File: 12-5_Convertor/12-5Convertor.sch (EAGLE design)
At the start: 19 parts, among them IC1 ACS764, U1 LM2678

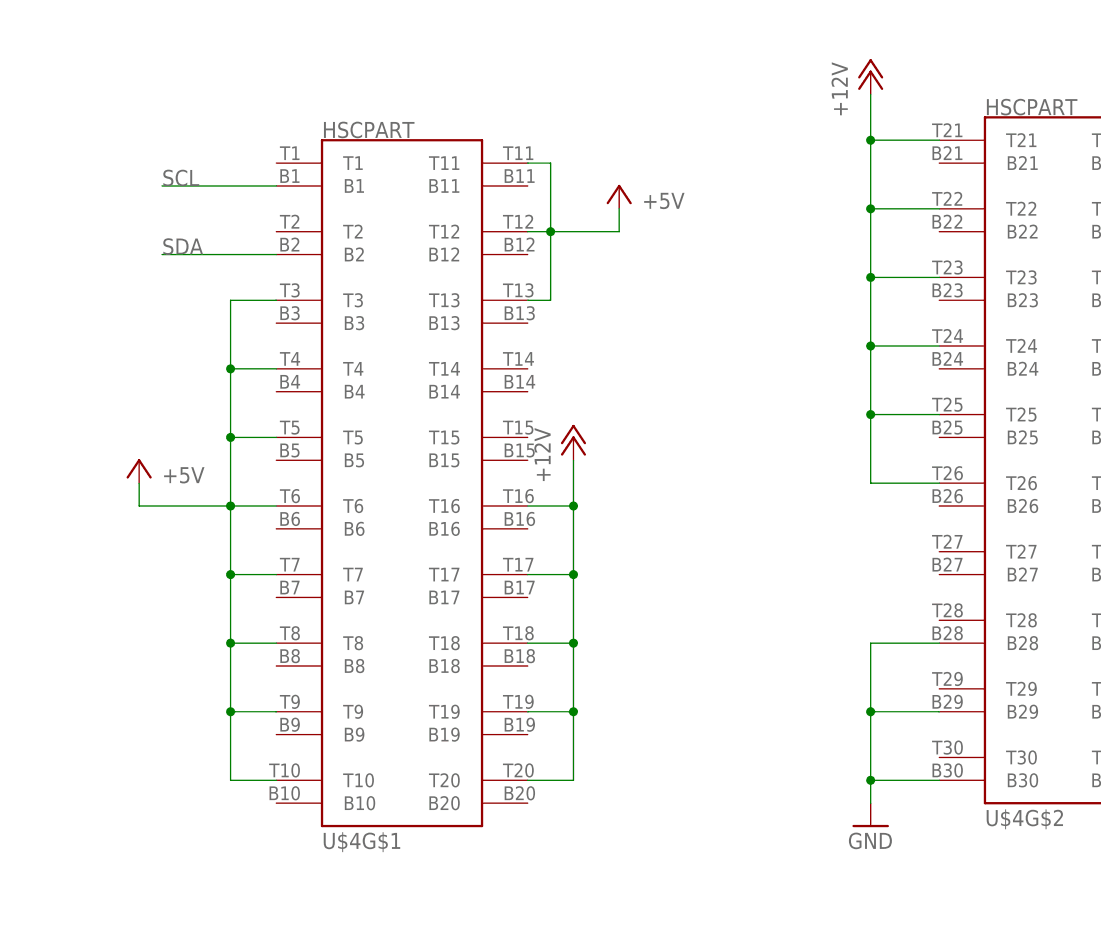
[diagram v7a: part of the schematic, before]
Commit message: Changed the pin order of the backplane connector
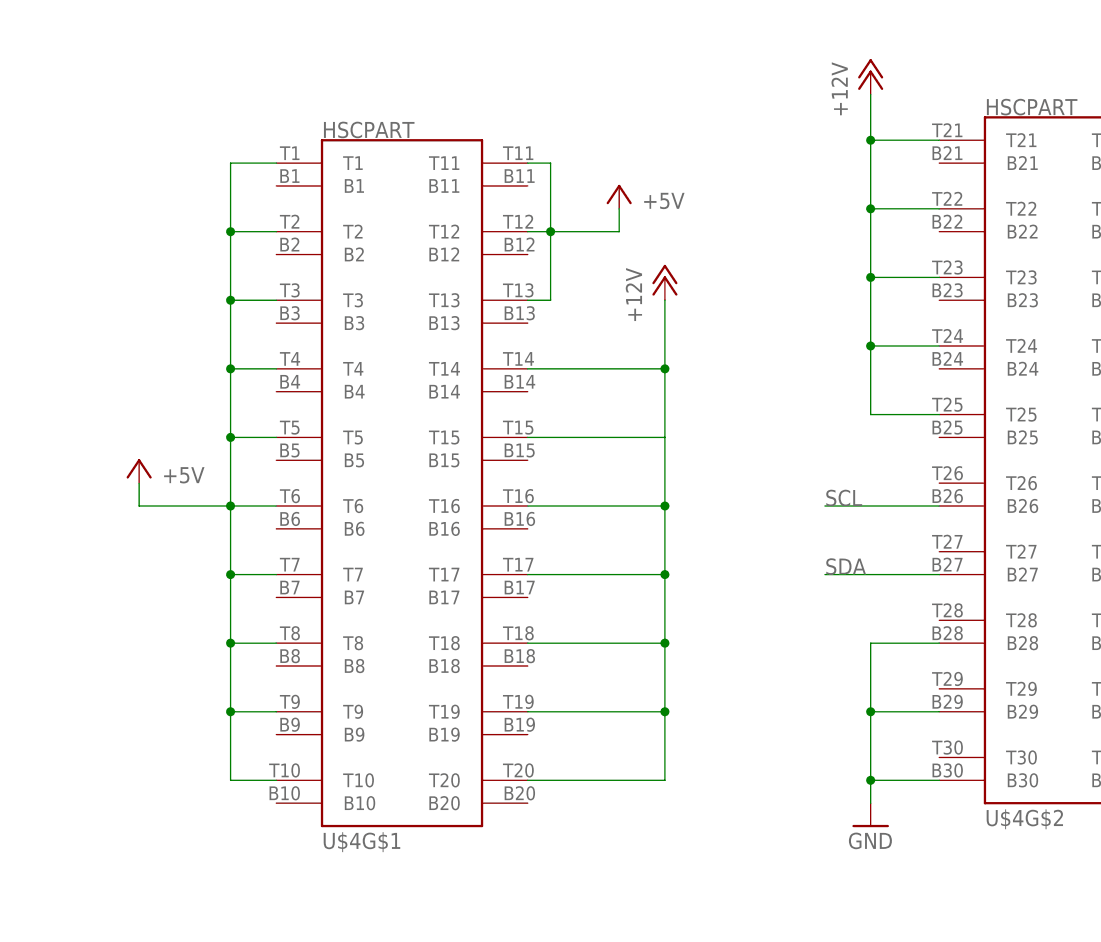
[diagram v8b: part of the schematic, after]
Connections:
- net +12V: now also U$4G$1.T14, U$4G$1.T15; no longer U$4G$2.T26
- net +5V: now also U$4G$1.T1, U$4G$1.T2
- net SCL: now also U$4G$2.B26; no longer U$4G$1.B1
- net SDA: now also U$4G$2.B27; no longer U$4G$1.B2
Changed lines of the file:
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@@
 <?xml version="1.0" encoding="utf-8"?>
 <!DOCTYPE eagle SYSTEM "eagle.dtd">
-<eagle version="7.5.0">
+<eagle version="7.2.0">
 <drawing>
 <settings>
@@
 </instance>
 <instance part="P+6" gate="1" x="271.78" y="203.2"/>
-<instance part="P+7" gate="1" x="238.76" y="162.56"/>
+<instance part="P+7" gate="1" x="248.92" y="180.34"/>
 <instance part="GND4" gate="1" x="271.78" y="119.38" smashed="yes">
 <attribute name="VALUE" x="269.24" y="116.84" size="1.778" layer="96"/>
@@
 <segment>
 <pinref part="U$4" gate="G$1" pin="T16"/>
-<wire x1="233.68" y1="154.94" x2="238.76" y2="154.94" width="0.1524" layer="91"/>
-<wire x1="238.76" y1="154.94" x2="238.76" y2="147.32" width="0.1524" layer="91"/>
+<wire x1="233.68" y1="154.94" x2="248.92" y2="154.94" width="0.1524" layer="91"/>
+<wire x1="248.92" y1="154.94" x2="248.92" y2="147.32" width="0.1524" layer="91"/>
 <pinref part="U$4" gate="G$1" pin="T17"/>
-<wire x1="238.76" y1="147.32" x2="233.68" y2="147.32" width="0.1524" layer="91"/>
-<wire x1="238.76" y1="147.32" x2="238.76" y2="139.7" width="0.1524" layer="91"/>
-<junction x="238.76" y="147.32"/>
+<wire x1="248.92" y1="147.32" x2="233.68" y2="147.32" width="0.1524" layer="91"/>
+<wire x1="248.92" y1="147.32" x2="248.92" y2="139.7" width="0.1524" layer="91"/>
+<junction x="248.92" y="147.32"/>
 <pinref part="U$4" gate="G$1" pin="T18"/>
-<wire x1="238.76" y1="139.7" x2="233.68" y2="139.7" width="0.1524" layer="91"/>
-<wire x1="238.76" y1="139.7" x2="238.76" y2="132.08" width="0.1524" layer="91"/>
-<junction x="238.76" y="139.7"/>
+<wire x1="248.92" y1="139.7" x2="233.68" y2="139.7" width="0.1524" layer="91"/>
+<pinref part="P+7" gate="1" pin="+12V"/>
+<wire x1="248.92" y1="177.8" x2="248.92" y2="170.18" width="0.1524" layer="91"/>
+<junction x="248.92" y="154.94"/>
+<pinref part="U$4" gate="G$1" pin="T14"/>
+<wire x1="248.92" y1="170.18" x2="248.92" y2="162.56" width="0.1524" layer="91"/>
+<wire x1="248.92" y1="162.56" x2="248.92" y2="154.94" width="0.1524" layer="91"/>
+<wire x1="233.68" y1="170.18" x2="248.92" y2="170.18" width="0.1524" layer="91"/>
+<junction x="248.92" y="170.18"/>
+<pinref part="U$4" gate="G$1" pin="T15"/>
+<wire x1="233.68" y1="162.56" x2="248.92" y2="162.56" width="0.1524" layer="91"/>
 <pinref part="U$4" gate="G$1" pin="T19"/>
-<wire x1="238.76" y1="132.08" x2="233.68" y2="132.08" width="0.1524" layer="91"/>
-<wire x1="238.76" y1="132.08" x2="238.76" y2="124.46" width="0.1524" layer="91"/>
-<junction x="238.76" y="132.08"/>
+<wire x1="233.68" y1="132.08" x2="248.92" y2="132.08" width="0.1524" layer="91"/>
+<wire x1="248.92" y1="132.08" x2="248.92" y2="139.7" width="0.1524" layer="91"/>
+<junction x="248.92" y="139.7"/>
 <pinref part="U$4" gate="G$1" pin="T20"/>
-<wire x1="238.76" y1="124.46" x2="233.68" y2="124.46" width="0.1524" layer="91"/>
-<pinref part="P+7" gate="1" pin="+12V"/>
-<wire x1="238.76" y1="160.02" x2="238.76" y2="154.94" width="0.1524" layer="91"/>
-<junction x="238.76" y="154.94"/>
+<wire x1="233.68" y1="124.46" x2="248.92" y2="124.46" width="0.1524" layer="91"/>
+<wire x1="248.92" y1="124.46" x2="248.92" y2="132.08" width="0.1524" layer="91"/>
+<junction x="248.92" y="132.08"/>
 </segment>
 <segment>
@@
 <pinref part="U$4" gate="G$2" pin="T25"/>
 <wire x1="271.78" y1="165.1" x2="279.4" y2="165.1" width="0.1524" layer="91"/>
-<wire x1="271.78" y1="165.1" x2="271.78" y2="157.48" width="0.1524" layer="91"/>
-<junction x="271.78" y="165.1"/>
-<pinref part="U$4" gate="G$2" pin="T26"/>
-<wire x1="271.78" y1="157.48" x2="279.4" y2="157.48" width="0.1524" layer="91"/>
 <pinref part="P+6" gate="1" pin="+12V"/>
 <wire x1="271.78" y1="200.66" x2="271.78" y2="195.58" width="0.1524" layer="91"/>
@@
 <pinref part="P+5" gate="1" pin="+5V"/>
 <wire x1="190.5" y1="154.94" x2="190.5" y2="157.48" width="0.1524" layer="91"/>
+<wire x1="200.66" y1="177.8" x2="200.66" y2="185.42" width="0.1524" layer="91"/>
+<junction x="200.66" y="177.8"/>
+<pinref part="U$4" gate="G$1" pin="T2"/>
+<wire x1="200.66" y1="185.42" x2="205.74" y2="185.42" width="0.1524" layer="91"/>
+<wire x1="200.66" y1="185.42" x2="200.66" y2="193.04" width="0.1524" layer="91"/>
+<junction x="200.66" y="185.42"/>
+<pinref part="U$4" gate="G$1" pin="T1"/>
+<wire x1="200.66" y1="193.04" x2="205.74" y2="193.04" width="0.1524" layer="91"/>
 </segment>
 <segment>
@@
 <net name="SCL" class="0">
 <segment>
-<pinref part="U$4" gate="G$1" pin="B1"/>
-<wire x1="205.74" y1="190.5" x2="193.04" y2="190.5" width="0.1524" layer="91"/>
-<label x="193.04" y="190.5" size="1.778" layer="95"/>
-</segment>
-<segment>
 <pinref part="IC1" gate="G$1" pin="SCL"/>
 <wire x1="60.96" y1="129.54" x2="53.34" y2="129.54" width="0.1524" layer="91"/>
 <label x="53.34" y="129.54" size="1.778" layer="95"/>
 </segment>
+<segment>
+<pinref part="U$4" gate="G$2" pin="B26"/>
+<wire x1="279.4" y1="154.94" x2="266.7" y2="154.94" width="0.1524" layer="91"/>
+<label x="266.7" y="154.94" size="1.778" layer="95"/>
+</segment>
 </net>
 <net name="SDA" class="0">
-<segment>
-<pinref part="U$4" gate="G$1" pin="B2"/>
-<wire x1="205.74" y1="182.88" x2="193.04" y2="182.88" width="0.1524" layer="91"/>
-<label x="193.04" y="182.88" size="1.778" layer="95"/>
-</segment>
 <segment>
 <pinref part="IC1" gate="G$1" pin="SDA"/>
@@
 <label x="53.34" y="132.08" size="1.778" layer="95"/>
 </segment>
-</net>
+<segment>
+<pinref part="U$4" gate="G$2" pin="B27"/>
+<wire x1="279.4" y1="147.32" x2="266.7" y2="147.32" width="0.1524" layer="91"/>
+<label x="266.7" y="147.32" size="1.778" layer="95"/>
+</segment>
+</net>
